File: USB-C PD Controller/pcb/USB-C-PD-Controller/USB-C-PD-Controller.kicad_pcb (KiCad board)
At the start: 2 copper layers, 52.1 x 24.1 mm, 35 parts, among them J1 Conn_02x04_Odd_Even, J2 Conn_02x04_Odd_Even, J201 USB_C_Receptacle_USB2.0_16P, Q201 IRF9358, Q202 2N7002, Q203 BSL308PE, U201 USBLC6-2SC6, U202 CYPD3177-24LQ

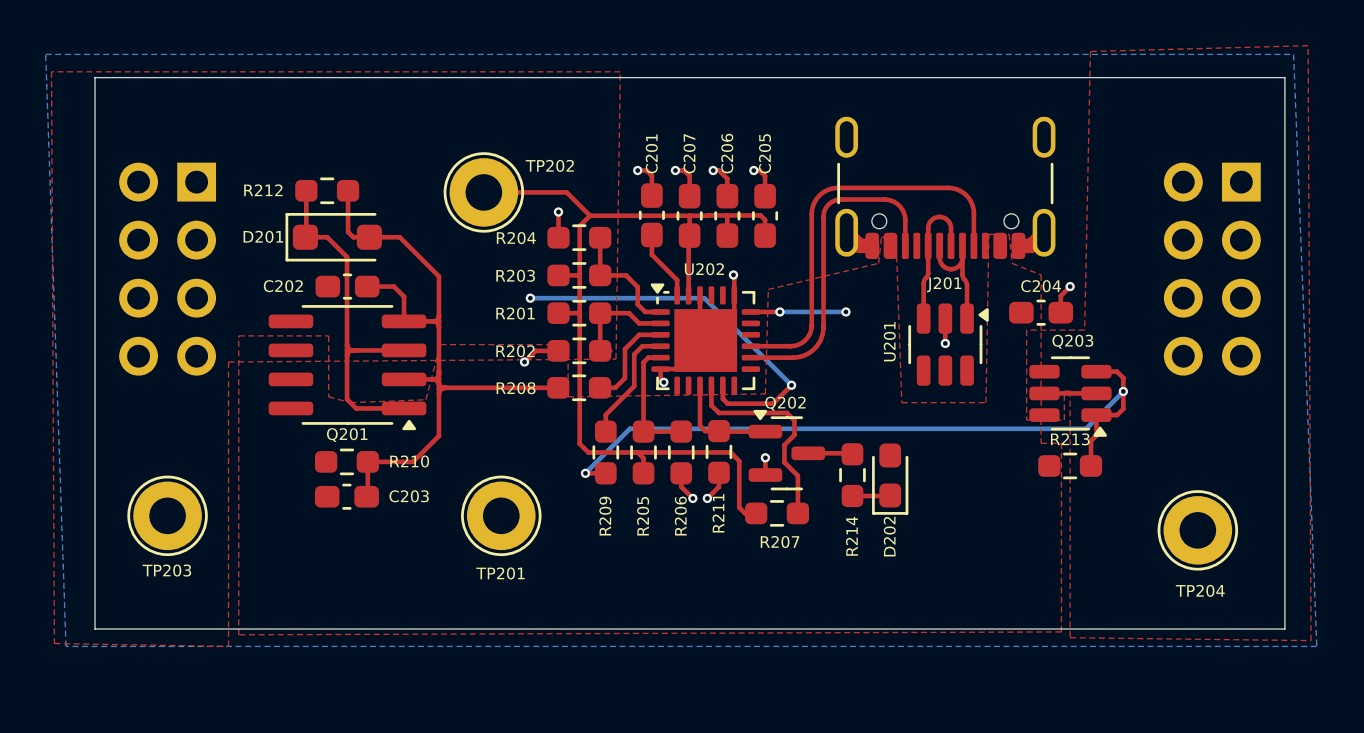
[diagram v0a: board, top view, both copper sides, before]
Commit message: USB-C PD Controller finishing touches
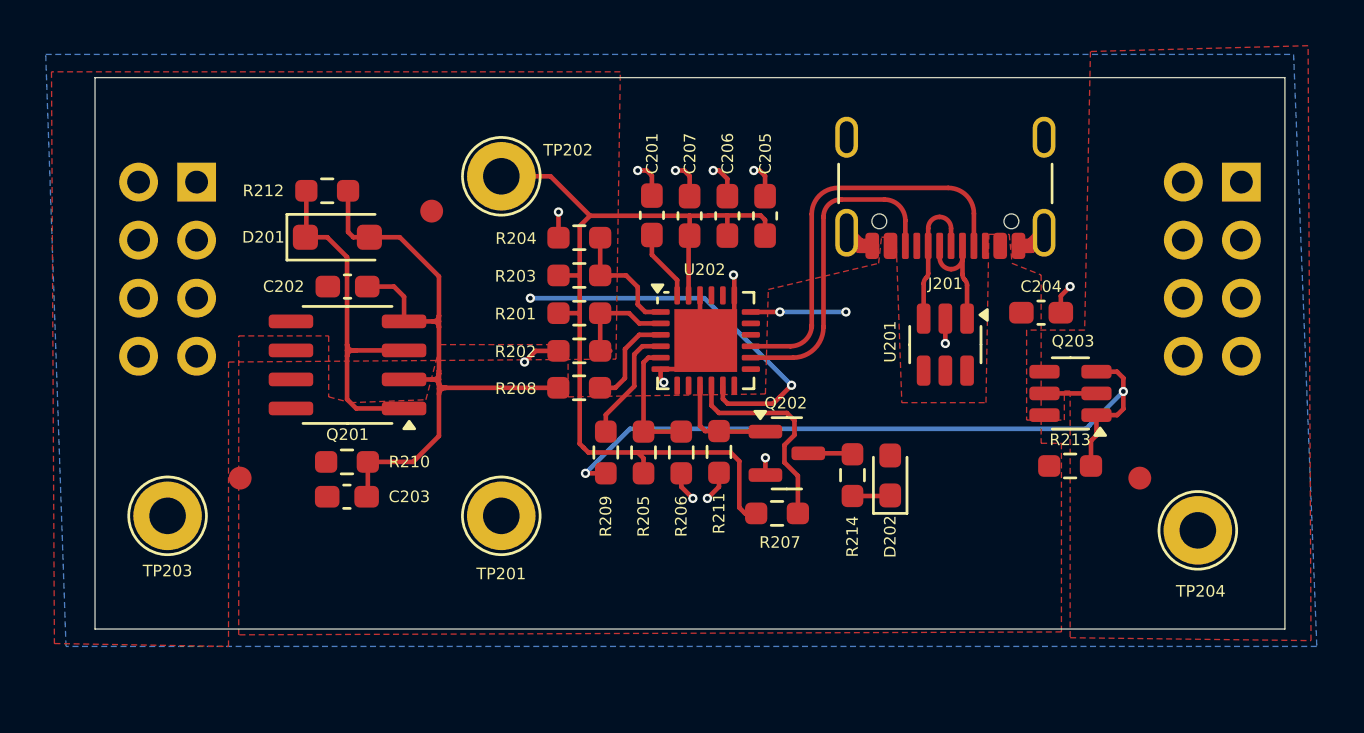
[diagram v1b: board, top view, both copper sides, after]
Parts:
- added FID1: Fiducial, Fiducial:Fiducial_1mm_Mask2mm, F.Cu at (123.6, 110.1)
- added FID2: Fiducial, Fiducial:Fiducial_1mm_Mask2mm, F.Cu at (115.2, 121.8)
- added FID3: Fiducial, Fiducial:Fiducial_1mm_Mask2mm, F.Cu at (154.6, 121.8)
- added G***: LOGO, LOGO, B.Cu at (135.5, 115.7)
- moved TP202 1.04 mm to (126.6, 108.6)
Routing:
- net /USB-C PD Controller/VDDD: track 42.2 -> 41.2 mm
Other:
- board text added: "USB-C PD Controller Rev. 1"

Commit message: USB-C PD Controller fabrication outputs
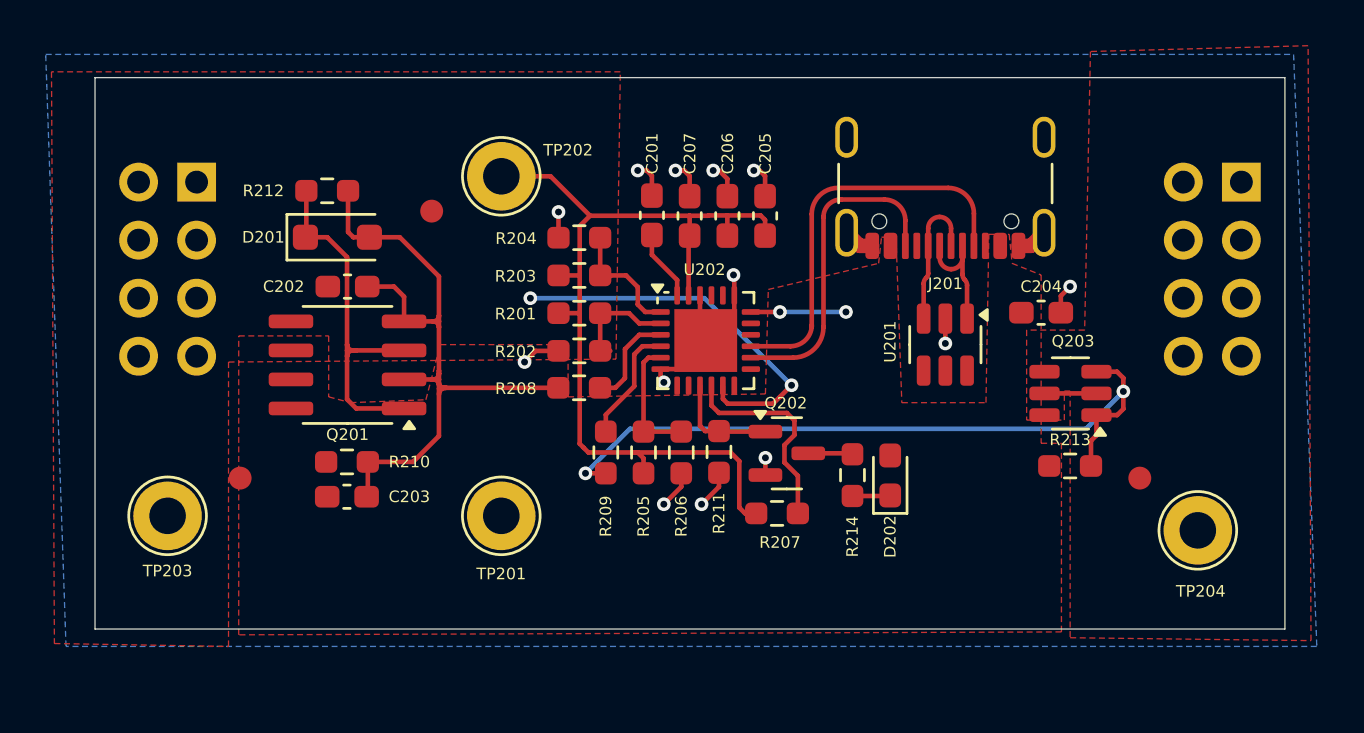
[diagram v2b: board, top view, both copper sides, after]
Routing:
- net GNDD: track 26.1 -> 26.9 mm
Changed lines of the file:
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@@
 			(outputformat 1)
 			(mirror no)
-			(drillshape 1)
+			(drillshape 0)
 			(scaleselection 1)
-			(outputdirectory "")
+			(outputdirectory "../../fab/rev-1/gerbers/")
 		)
 	)
@@
 	)
 	(segment
+		(start 135.382 122.9595)
+		(end 136.144 122.1975)
+		(width 0.2032)
+		(layer "F.Cu")
+		(net 1)
+	)
+	(segment
 		(start 134.859 108.5935)
 		(end 134.859 109.478873)
@@
 	)
 	(segment
-		(start 151.1035 113.842)
-		(end 151.1035 114.5775)
+		(start 136.144 122.1975)
+		(end 136.144 121.582873)
 		(width 0.2032)
 		(layer "F.Cu")
@@
 	)
 	(segment
-		(start 128.122627 116.248873)
-		(end 127.635 116.7365)
+		(start 133.731 122.9595)
+		(end 134.493 122.1975)
 		(width 0.2032)
 		(layer "F.Cu")
@@
 	)
 	(segment
-		(start 136.144 122.1975)
-		(end 135.636 122.7055)
+		(start 151.1035 113.842)
+		(end 151.1035 114.5775)
+		(width 0.2032)
+		(layer "F.Cu")
+		(net 1)
+	)
+	(segment
+		(start 128.122627 116.248873)
+		(end 127.635 116.7365)
 		(width 0.2032)
 		(layer "F.Cu")
@@
 	)
 	(segment
-		(start 136.144 121.582873)
-		(end 136.144 122.1975)
-		(width 0.2032)
-		(layer "F.Cu")
-		(net 1)
-	)
-	(segment
 		(start 146.05 115.924094)
 		(end 146.05 114.837)
@@
 	)
 	(segment
-		(start 135.001 122.7055)
-		(end 134.493 122.1975)
-		(width 0.2032)
-		(layer "F.Cu")
-		(net 1)
-	)
-	(segment
 		(start 151.511 113.4345)
 		(end 151.1035 113.842)
@@
 	(via
 		(at 132.588 108.3545)
-		(size 0.4064)
-		(drill 0.2032)
+		(size 0.6)
+		(drill 0.3)
 		(layers "F.Cu" "B.Cu")
 		(free yes)
@@
 	(via
 		(at 129.1205 110.171)
-		(size 0.4064)
-		(drill 0.2032)
+		(size 0.6)
+		(drill 0.3)
 		(layers "F.Cu" "B.Cu")
 		(net 1)
@@
 	(via
 		(at 137.668 108.3545)
-		(size 0.4064)
-		(drill 0.2032)
+		(size 0.6)
+		(drill 0.3)
 		(layers "F.Cu" "B.Cu")
 		(free yes)
@@
 	(via
 		(at 127.635 116.7365)
-		(size 0.4064)
-		(drill 0.2032)
+		(size 0.6)
+		(drill 0.3)
 		(layers "F.Cu" "B.Cu")
 		(net 1)
@@
 	(via
 		(at 135.89 108.3545)
-		(size 0.4064)
-		(drill 0.2032)
+		(size 0.6)
+		(drill 0.3)
 		(layers "F.Cu" "B.Cu")
 		(free yes)
@@
 	(via
 		(at 133.731 117.6255)
-		(size 0.4064)
-		(drill 0.2032)
+		(size 0.6)
+		(drill 0.3)
 		(layers "F.Cu" "B.Cu")
 		(free yes)
@@
 	(via
 		(at 146.05 115.924094)
-		(size 0.4064)
-		(drill 0.2032)
+		(size 0.6)
+		(drill 0.3)
 		(layers "F.Cu" "B.Cu")
 		(net 1)
 	)
 	(via
-		(at 135.001 122.7055)
-		(size 0.4064)
-		(drill 0.2032)
+		(at 133.731 122.9595)
+		(size 0.6)
+		(drill 0.3)
 		(layers "F.Cu" "B.Cu")
 		(free yes)
@@
 	(via
 		(at 138.176 120.9275)
-		(size 0.4064)
-		(drill 0.2032)
+		(size 0.6)
+		(drill 0.3)
 		(layers "F.Cu" "B.Cu")
 		(net 1)
@@
 	(via
 		(at 136.779 112.9265)
-		(size 0.4064)
-		(drill 0.2032)
+		(size 0.6)
+		(drill 0.3)
 		(layers "F.Cu" "B.Cu")
 		(free yes)
@@
 	(via
 		(at 151.511 113.4345)
-		(size 0.4064)
-		(drill 0.2032)
+		(size 0.6)
+		(drill 0.3)
 		(layers "F.Cu" "B.Cu")
 		(net 1)
 	)
 	(via
-		(at 135.636 122.7055)
-		(size 0.4064)
-		(drill 0.2032)
+		(at 135.382 122.9595)
+		(size 0.6)
+		(drill 0.3)
 		(layers "F.Cu" "B.Cu")
 		(free yes)
@@
 	(via
 		(at 134.239 108.3545)
-		(size 0.4064)
-		(drill 0.2032)
+		(size 0.6)
+		(drill 0.3)
 		(layers "F.Cu" "B.Cu")
 		(free yes)
@@
 	(via
 		(at 127.889 113.9425)
-		(size 0.4064)
-		(drill 0.2032)
+		(size 0.6)
+		(drill 0.3)
 		(layers "F.Cu" "B.Cu")
 		(free yes)
@@
 	(via
 		(at 139.319 117.7525)
-		(size 0.4064)
-		(drill 0.2032)
+		(size 0.6)
+		(drill 0.3)
 		(layers "F.Cu" "B.Cu")
 		(net 3)
@@
 	(via
 		(at 141.700373 114.545873)
-		(size 0.4064)
-		(drill 0.2032)
+		(size 0.6)
+		(drill 0.3)
 		(layers "F.Cu" "B.Cu")
 		(net 5)
@@
 	(via
 		(at 138.811 114.545873)
-		(size 0.4064)
-		(drill 0.2032)
+		(size 0.6)
+		(drill 0.3)
 		(layers "F.Cu" "B.Cu")
 		(net 5)
@@
 	(via
 		(at 130.302 121.606373)
-		(size 0.4064)
-		(drill 0.2032)
+		(size 0.6)
+		(drill 0.3)
 		(layers "F.Cu" "B.Cu")
 		(net 17)
@@
 	(via
 		(at 153.84 118.0255)
-		(size 0.4064)
-		(drill 0.2032)
+		(size 0.6)
+		(drill 0.3)
 		(layers "F.Cu" "B.Cu")
 		(net 17)

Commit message: USB-C PD controller modifications because I can't make up my mind
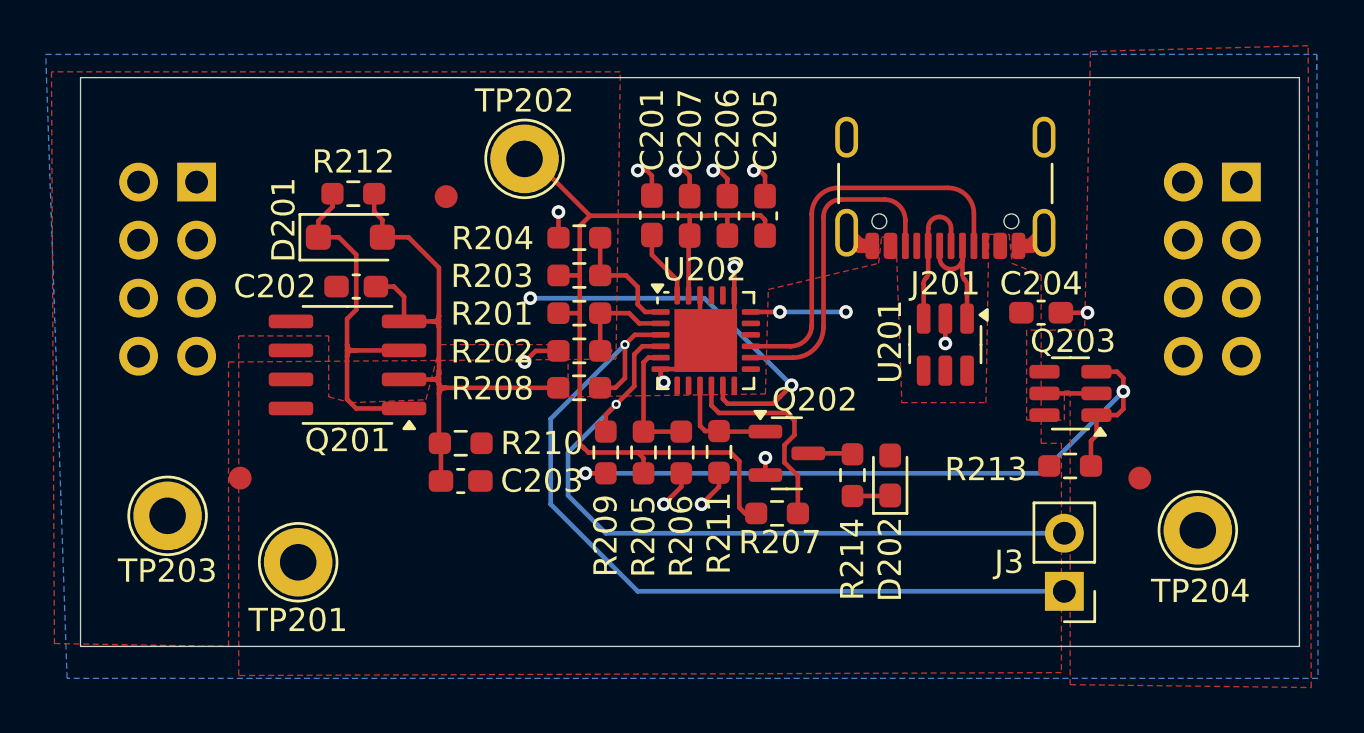
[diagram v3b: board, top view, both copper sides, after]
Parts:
- added J3: Conn_01x02_Pin, Connector_PinHeader_2.54mm:PinHeader_1x02_P2.54mm_Vertical, F.Cu at (151.3, 126.8)
- moved TP201 9.12 mm to (117.7, 125.5)
- moved R210 5.04 mm to (124.8, 120.3), turned to 180 degrees
- moved C203 5.03 mm to (124.8, 121.9), turned to 180 degrees
- moved TP202 1.27 mm to (127.6, 107.8)
- moved R212 1.15 mm to (120.1, 109.4)
- moved FID1 0.90 mm to (124.2, 109.5)
- moved D201 0.57 mm to (120.0, 111.3)
- moved C202 0.38 mm to (120.3, 113.4)
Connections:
- net Net-(U202-SAFE_PWR_EN) renamed /USB-C PD Controller/SAFE_PWR_EN
- net Net-(U202-VBUS_FET_EN) renamed /USB-C PD Controller/VBUS_FET_EN
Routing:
- net /USB-C PD Controller/VBUS_FET_EN: track 3.96 -> 36.5 mm, vias 0 -> 1
- net /USB-C PD Controller/SAFE_PWR_EN: track 5.20 -> 32.5 mm, vias 0 -> 1
- net Net-(D201-A): track 32.4 -> 27.9 mm
- net /USB-C PD Controller/VDDD: track 41.2 -> 40.5 mm
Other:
- board size 52.1 x 24.1 mm -> 53.3 x 24.9 mm
